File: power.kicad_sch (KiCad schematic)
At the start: 20 parts, among them J1 1054500101, J2 S2B-PH-SM4-TB, U3 BQ25601, U4 XC6210B332MR, U5 XC6210B182MR

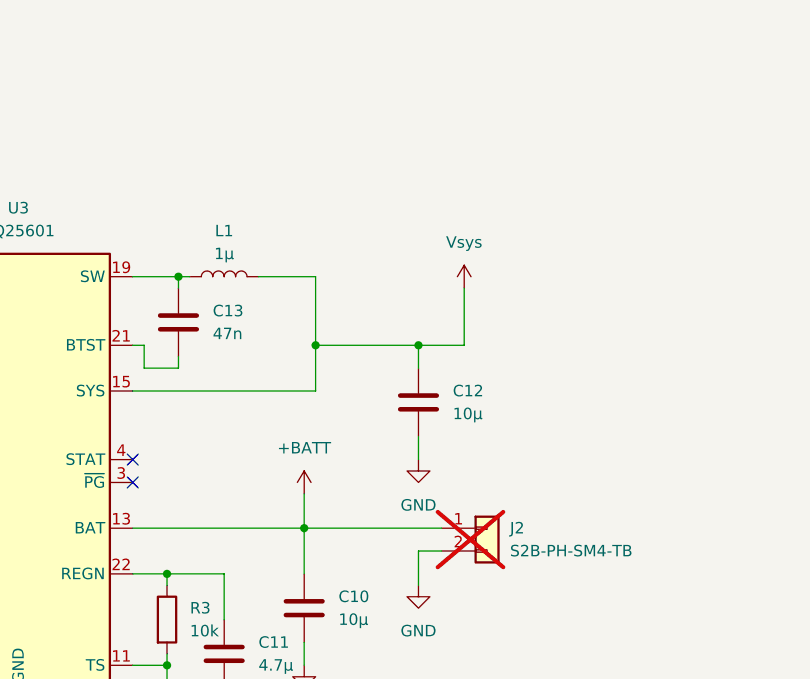
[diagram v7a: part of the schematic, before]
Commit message: Add red and IR LED for capter
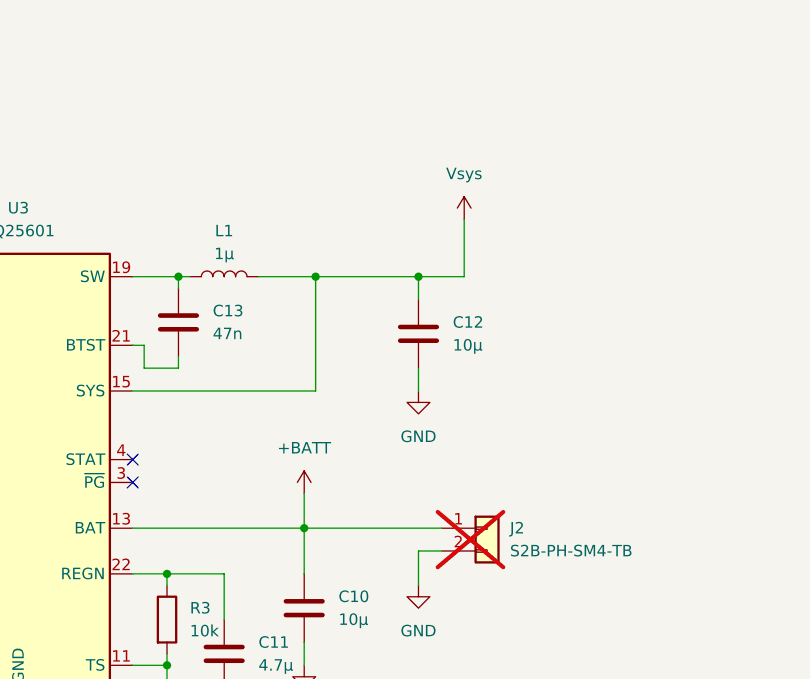
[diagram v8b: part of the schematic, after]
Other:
- moved on the sheet: C12
